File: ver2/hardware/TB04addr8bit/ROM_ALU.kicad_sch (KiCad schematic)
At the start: 27 parts, among them IC9 74HC161N, U10 74LS08, U11 74LS273, U14 74HC238, U20 74HC273, U21 74HC74, U22 74HC273, U24 28C256, U5 28C256

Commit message: ver2: 回路図の要修正5件を修正しアノテーションを掛け直し
- 74HC193(旧U39/新U38)の~CO・~BOをVDD直結から開放に(出力短絡の回避)
- 電源未接続だった4IC(74HC00/74LS32/74AHC04/74LS08)にVCC/GNDを配線
  し、バイパスコンデンサ0.1u×4を追加
- ネット名 Decord を DCR に統一(デコーダ制御信号のラッチ不成立を解消)
- PC_LAOD の綴りを PC_LOAD に修正
- 書込デコーダ138の入力を OPR8-10 から sel_a0-2 へ付け替え
  (LD Ri,[Im8] が別レジスタに書く不具合の解消)
- ver1基板由来だった参照記号をアノテーション掛け直しで整理
  (部品216個・名前付きネット146本とも掛け直し前後で一致、ERCも同数)
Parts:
- renumbered C31 to C37, C6 to C38, C20 to C39, C34 to C40, C24 to C41, C23 to C42, C28 to C43, C30 to C44, D43 to D36, D42 to D37, D40 to D39, D41 to D40, D39 to D41, IC9 to IC13, R22 to R15, R21 to R16, RN8 to RN5, U11 to U21, U24 to U22, U5 to U23, U21 to U24, U10 to U25, U22 to U26, U14 to U27

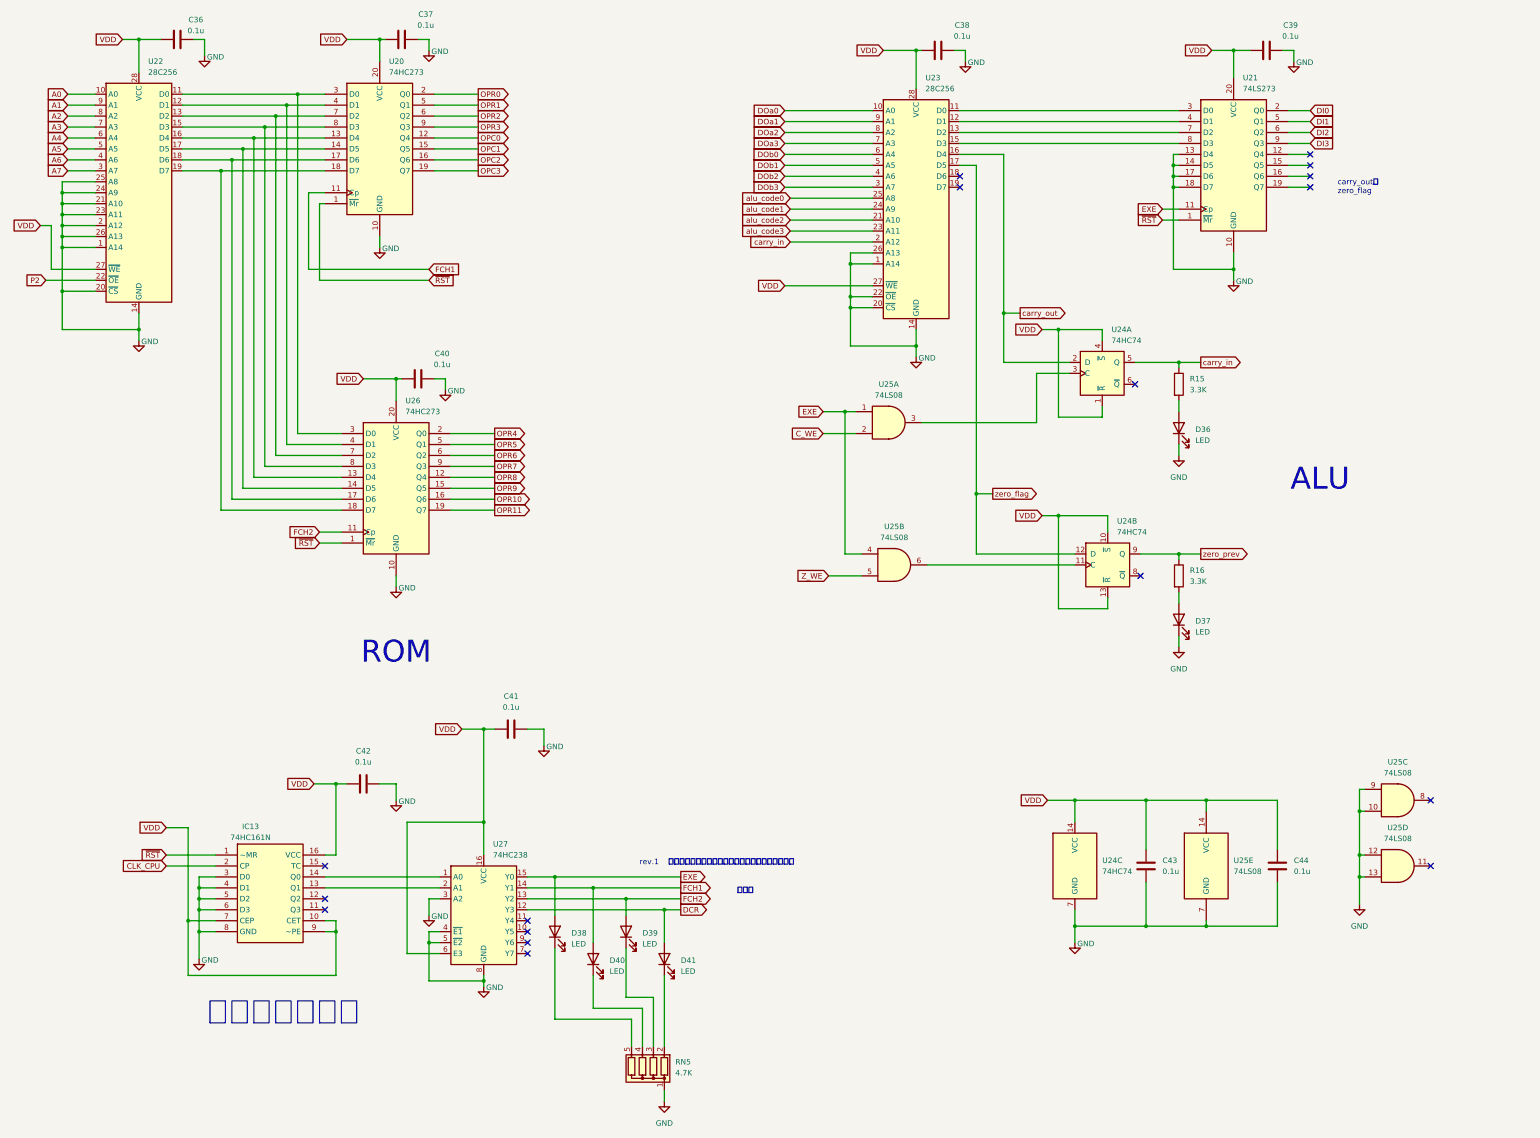
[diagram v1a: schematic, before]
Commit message: ver2: addrMUXシートを新設、リセット起点をFCH1へ、mAddr専用レジスタを廃止
- addrMUX.kicad_sch を新設。74HC138(U41)で SEL_M からアドレス源の
  イネーブルをワンホット生成し、74HC244×5(U42-U46)を配置
  mAddr用(U43)の入力は byte2ラッチのOPR4-11から直取り
- mAddr専用レジスタ(IC11/IC12)を削除。byte2ラッチが mAddr を兼ねる
  これまで消費先ゼロだった OPR7/OPR11 の浮きも解消
- 74HC238の出力割付を1つ回してリセット起点を EXE から FCH1 へ
  (Y0=FCH1/Y1=FCH2/Y2=DCR/Y3=EXE、相順は不変)
- PCの161はCEPを共通イネーブルに揃え、桁上げをTC->CETで接続

未了: 命令ラッチの取り込みエッジを1相ずらす変更(U20 Cp=FCH2 /
U26 Cp=DCR)。EXE中はアドレスバスがmAddrのため、現状のままでは
EXE->FCH1の境目でROMのアクセスが間に合わない
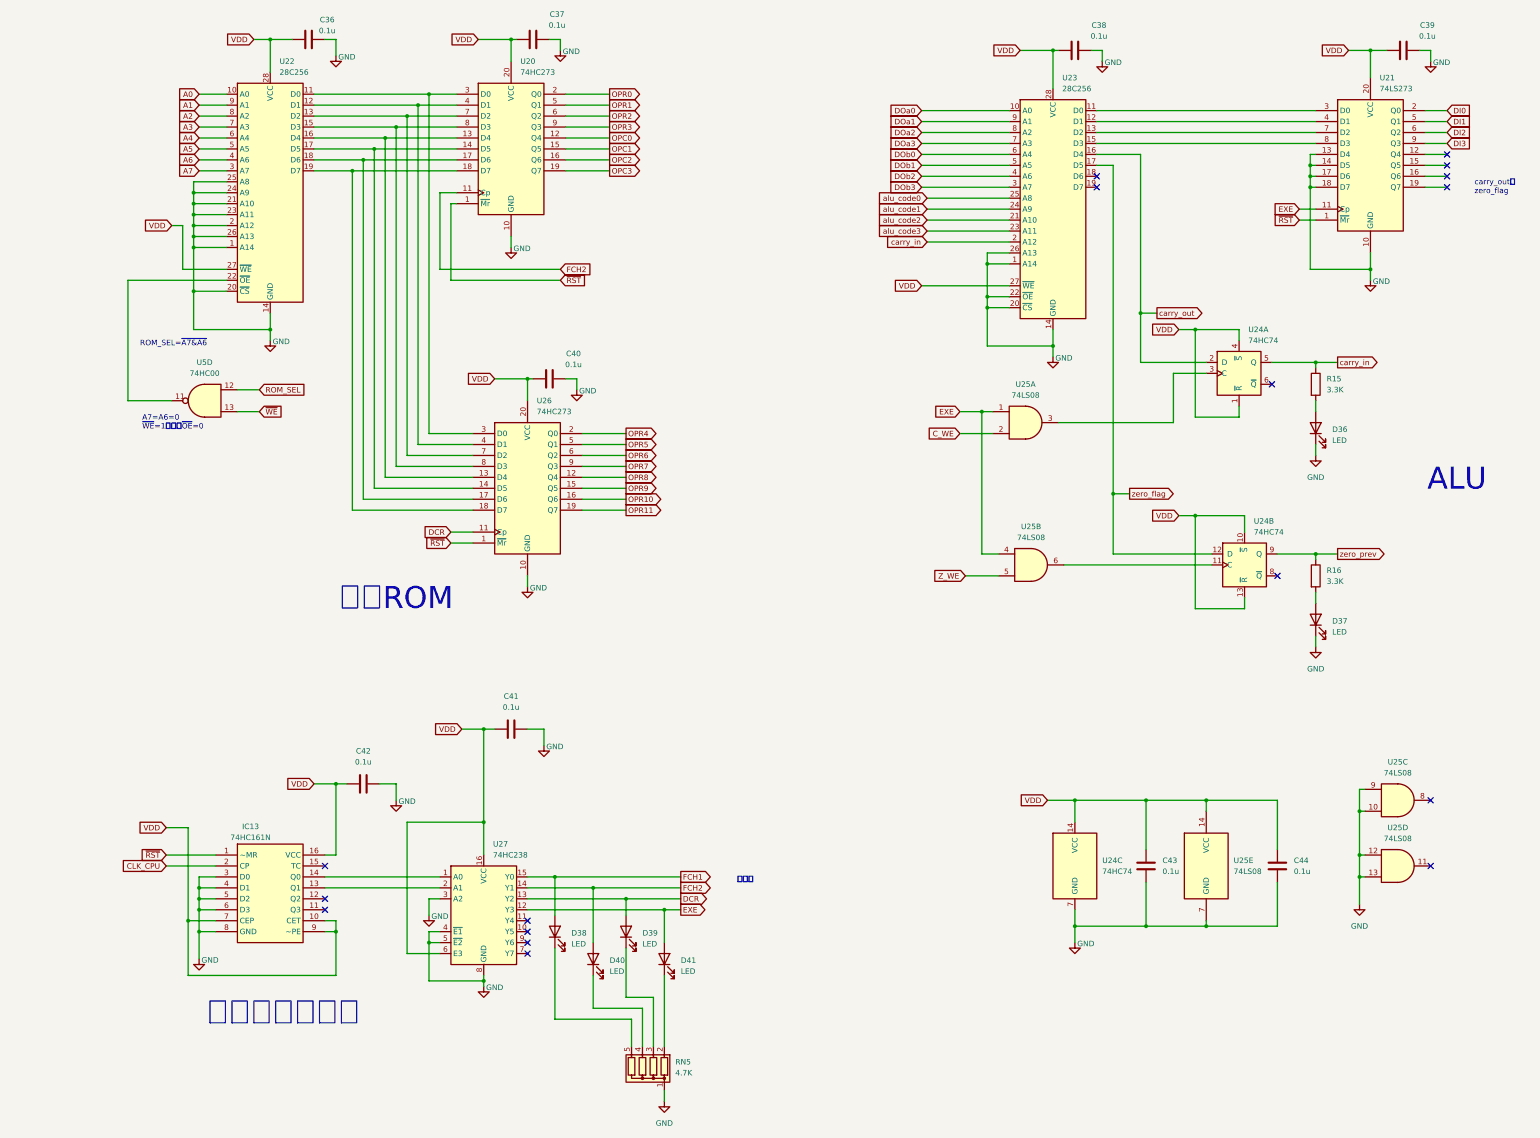
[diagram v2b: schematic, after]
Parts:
- added U5: 74HC00, symbol 74xx:74HC00
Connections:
- net DCR: now also D39.2 (A), U26.11 (Cp), U27.13 (Y2); no longer D41.2 (A), U27.12 (Y3)
- net EXE: now also D41.2 (A), U27.12 (Y3); no longer D38.2 (A), U27.15 (Y0)
- net FCH1: now also D38.2 (A), U27.15 (Y0); no longer D40.2 (A), U20.11 (Cp), U27.14 (Y1)
- net FCH2: now also D40.2 (A), U20.11 (Cp), U27.14 (Y1); no longer D39.2 (A), U26.11 (Cp), U27.13 (Y2)
- net P2: no longer names the net of U22.22 (~{OE})
- net P2: now also U5.11
- new net ROM_SEL: U5.12
- new net ~{WE}: U5.13
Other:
- note added: "A7=A6=0 ~{WE}=1のとき~{OE}=0"
- note added: "ROM_SEL=~{A7&A6}"
- note added: "命令ROM"
- note removed: "ROM"
- note removed: "rev.1 １命令めでフェッチを確実にするために入れ替えた"
- moved on the sheet: C36, C37, C38, C39, C40, D36, D37, R15, R16, U20, U21, U22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
